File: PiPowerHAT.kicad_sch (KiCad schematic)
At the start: 31 parts, among them J3 Conn_01x02, J8 Conn_01x02

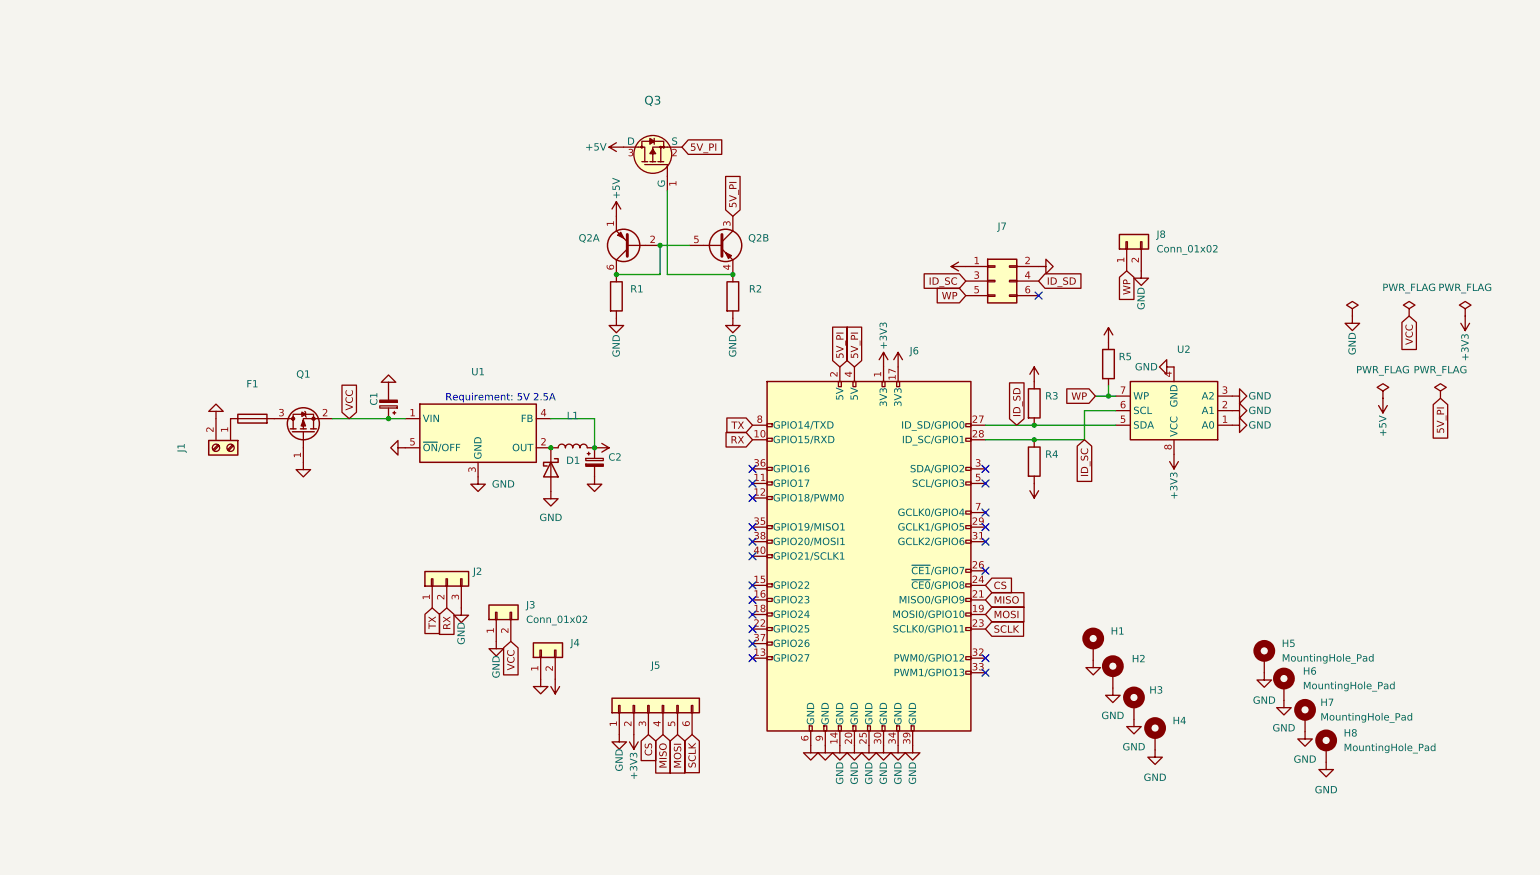
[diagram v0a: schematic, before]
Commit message: Updating to add freewheeling diodes, power LEDs, etc.
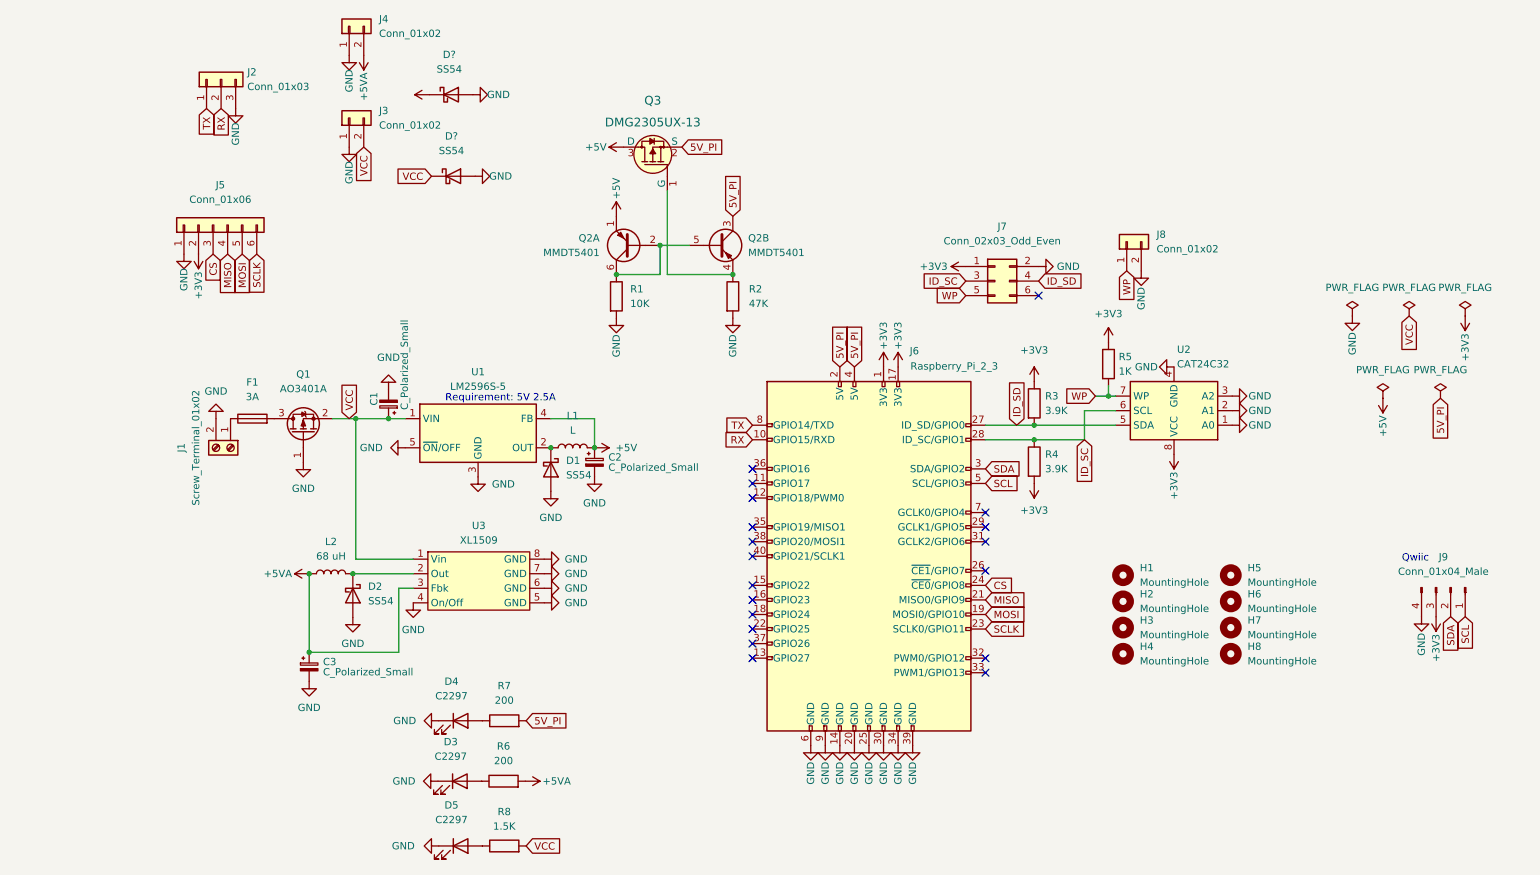
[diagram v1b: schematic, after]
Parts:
- removed H1, H2, H3, H4: (no value), symbol Mechanical:MountingHole_Pad
- removed H5, H6, H7, H8: MountingHole_Pad, symbol Mechanical:MountingHole_Pad
- added C3: C_Polarized_Small, symbol Device:C_Polarized_Small
- added D2, D? (x2): SS54, symbol Device:D_Schottky
- added D3, D4, D5: C2297, LED_SMD:LED_0805_2012Metric, symbol Device:LED
- added H1, H2, H3, H4, H5, H6, H7, H8: MountingHole, symbol Mechanical:MountingHole
- added J9: Conn_01x04_Male, symbol Connector:Conn_01x04_Male
- added L2: 68 uH, symbol Device:L
- added R6, R7: 200, symbol Device:R
- added R8: 1.5K, symbol Device:R
- added U3: XL1509, Package_SO:SOIC-8_3.9x4.9mm_P1.27mm, symbol Regulator_Switching:XL1509
- C1, C2: value (none) -> C_Polarized_Small
- D1: value (none) -> SS54
- F1: value (none) -> 3A
- J1: value (none) -> Screw_Terminal_01x02
- J2: value (none) -> Conn_01x03
- J4: value (none) -> Conn_01x02
- J5: value (none) -> Conn_01x06
- J6: value (none) -> Raspberry_Pi_2_3
- J7: value (none) -> Conn_02x03_Odd_Even
- L1: value (none) -> L
- Q1: value (none) -> AO3401A; footprint (none) -> Package_TO_SOT_SMD:SOT-23
- Q2: value (none) -> MMDT5401; footprint (none) -> Package_TO_SOT_SMD:SOT-363_SC-70-6
- Q3: value (none) -> DMG2305UX-13; footprint (none) -> digikey-footprints:SOT-23-3
- R1: value (none) -> 10K
- R2: value (none) -> 47K
- R3, R4: value (none) -> 3.9K
- R5: value (none) -> 1K
- U1: value (none) -> LM2596S-5; footprint (none) -> Package_TO_SOT_SMD:TO-263-5_TabPin3
- U2: value (none) -> CAT24C32
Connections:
- net +3V3: now also J9.3 (Pin_3)
- net +5V: no longer J4.2 (Pin_2)
- net 5V_PI: now also R7.2
- net GND: now also C3.2, D2.2 (A), D3.1 (K), D4.1 (K), D5.1 (K), D?.2 (A), D?.2 (A), J9.4 (Pin_4), U3.4 (On/Off), U3.5 (GND), U3.6 (GND), U3.7 (GND), U3.8 (GND)
- net VCC: now also D?.1 (K), R8.2, U3.1 (Vin)
- net SDA: now reaches J6.3 (SDA/GPIO2)
- net SDA: now also J9.2 (Pin_2)
- net SCL: now reaches J6.5 (SCL/GPIO3)
- net SCL: now also J9.1 (Pin_1)
- new net: D3.2 (A), R6.1
- new net: D2.1 (K), L2.2, U3.2 (Out)
- new net: D5.2 (A), R8.1
- new net: D4.2 (A), R7.1
- new net +5VA: C3.1, D?.1 (K), J4.2 (Pin_2), L2.1, R6.2, U3.3 (Fbk)
- no-connect marks 21 -> 19
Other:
- note added: "Qwiic"
- moved on the sheet: J2, J3, J4, J5

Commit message: adding footprints assignment to sch
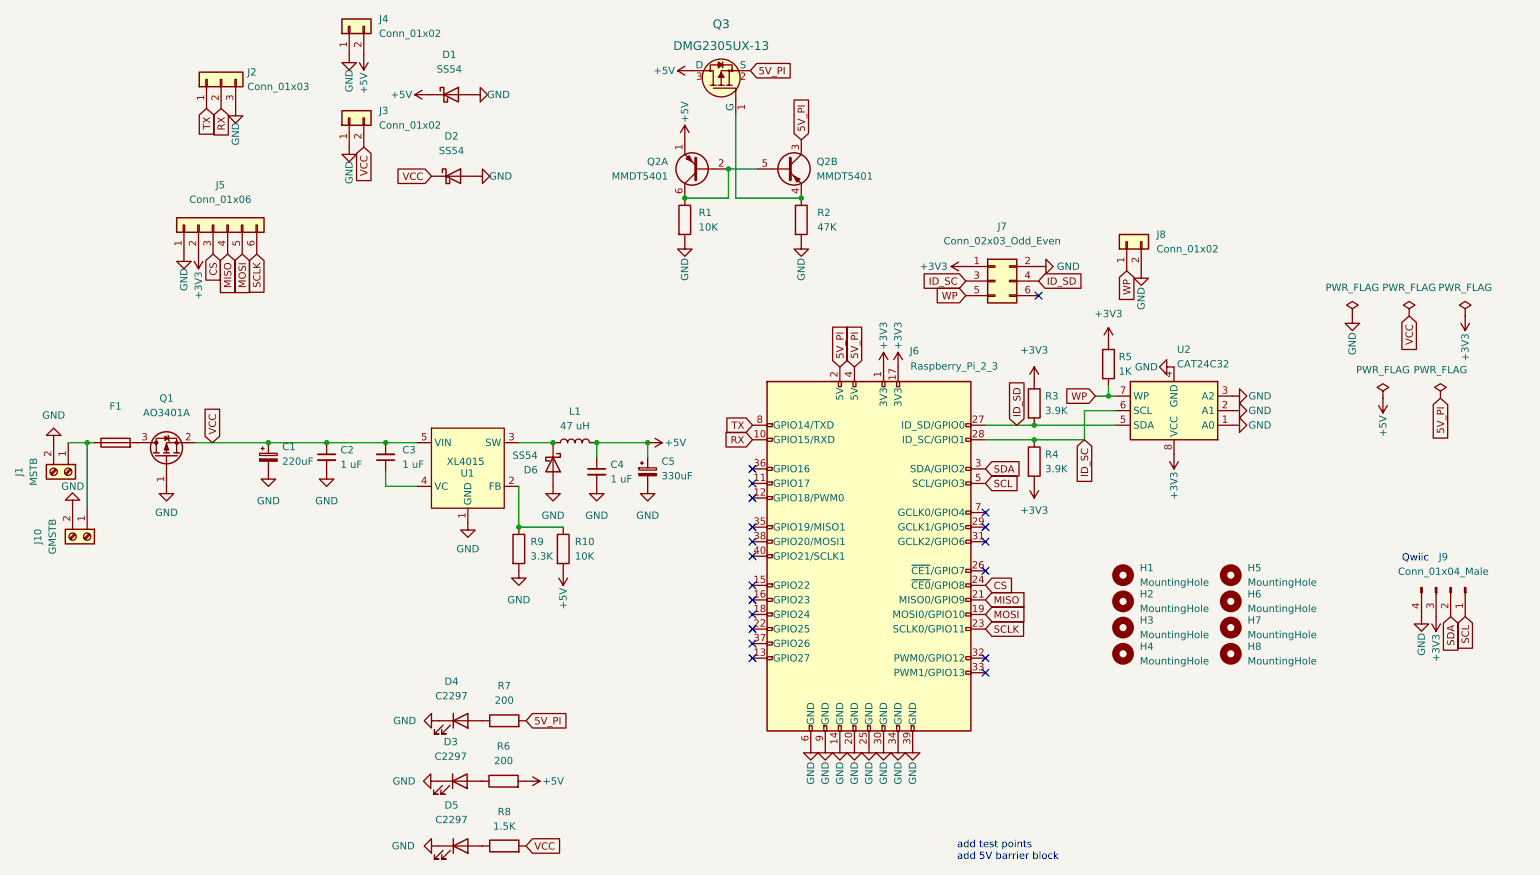
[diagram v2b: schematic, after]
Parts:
- removed C2, C3: C_Polarized_Small, symbol Device:C_Polarized_Small
- removed D1, D2: SS54, symbol Device:D_Schottky
- removed L2: 68 uH, symbol Device:L
- removed U1: LM2596S-5, Package_TO_SOT_SMD:TO-263-5_TabPin3, symbol Regulator_Switching:LM2596S-5
- removed U3: XL1509, Package_SO:SOIC-8_3.9x4.9mm_P1.27mm, symbol Regulator_Switching:XL1509
- added C2, C3, C4: 1 uF, Capacitor_SMD:C_0201_0603Metric, symbol Device:C_Small
- added C5: 330uF, Capacitor_SMD:CP_Elec_6.3x7.7, symbol Device:C_Polarized_Small
- added D6: SS54, Diode_SMD:D_SMA, symbol Device:D_Schottky
- added J10: GMSTB, Connector_Phoenix_GMSTB:PhoenixContact_GMSTBVA_2,5_2-G-7,62_1x02_P7.62mm_Vertical, symbol Connector:Screw_Terminal_01x02
- added R10: 10K, Resistor_SMD:R_0402_1005Metric, symbol Device:R
- added R9: 3.3K, Resistor_SMD:R_0402_1005Metric, symbol Device:R
- added U1: XL4015, Package_TO_SOT_SMD:TO-263-5_TabPin3, symbol Regulator_Switching:XL4015
- C1: value C_Polarized_Small -> 220uF; footprint (none) -> Capacitor_SMD:CP_Elec_10x10; JLC (none) -> C176670
- D1, D2: renamed from D?; footprint (none) -> Diode_SMD:D_SMA
- F1: value 3A -> (none); Farnell (none) -> 2292904
- H1, H2, H3, H4: footprint (none) -> MountingHole:MountingHole_2.7mm_M2.5_ISO14580
- H5, H6, H7, H8: footprint (none) -> MountingHole:MountingHole_3.5mm
- J1: value Screw_Terminal_01x02 -> MSTB; footprint (none) -> Connector_Phoenix_MSTB:PhoenixContact_MSTBVA_2,5_2-G_1x02_P5.00mm_Vertical
- J2: footprint (none) -> Connector_PinHeader_2.54mm:PinHeader_1x03_P2.54mm_Vertical
- J3, J4: footprint (none) -> Connector_JST:JST_XH_B2B-XH-AM_1x02_P2.50mm_Vertical
- J5: footprint (none) -> Connector_PinHeader_2.54mm:PinHeader_1x06_P2.54mm_Vertical
- J6: footprint (none) -> Connector_PinHeader_2.54mm:PinHeader_2x20_P2.54mm_Vertical
- J7: footprint (none) -> Connector_PinHeader_2.54mm:PinHeader_2x03_P2.54mm_Vertical_SMD
- J8: footprint (none) -> Connector_PinHeader_2.54mm:PinHeader_1x02_P2.54mm_Vertical
- J9: footprint (none) -> Connector_PinHeader_2.54mm:PinHeader_1x04_P2.54mm_Vertical
- L1: value L -> 47 uH; footprint (none) -> Inductor_SMD:L_12x12mm_H6mm; JLC (none) -> YSPI1365-470M
- R1: footprint (none) -> Resistor_SMD:R_0402_1005Metric
- R2: footprint (none) -> Resistor_SMD:R_0402_1005Metric; JLC (none) -> C25792
- R3, R4: footprint (none) -> Resistor_SMD:R_0402_1005Metric; JLC (none) -> C51721
- R5: footprint (none) -> Resistor_SMD:R_0402_1005Metric; JLC (none) -> C11702
- R6, R7: footprint (none) -> Resistor_SMD:R_0402_1005Metric; JLC (none) -> C25087
- R8: footprint (none) -> Resistor_SMD:R_0402_1005Metric; JLC (none) -> C25867
- U2: footprint (none) -> Package_SO:SOIC-8_3.9x4.9mm_P1.27mm
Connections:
- net +5VA is gone; now on net +5V: D1.1 (K), J4.2 (Pin_2), R6.2
- net +5V: now also C4.1, C5.1, R10.2
- net GND: now also C2.2, C4.2, C5.2, D6.2 (A), J10.2 (Pin_2), R9.2, U1.1 (GND)
- net VCC: now also C2.1, C3.2, U1.5 (VIN)
- net at F1.1, J1.1 (Pin_1): now also J10.1 (Pin_1)
- net at L1.1: now also D6.1 (K), U1.3 (SW)
- new net: C3.1, U1.4 (VC)
- new net: R10.1, R9.1, U1.2 (FB)
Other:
- note added: "add test points add 5V barrier block"
- note removed: "Requirement: 5V 2.5A"
- moved on the sheet: F1, J1, Q1, Q2A, Q2B, Q3, R1, R2

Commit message: currently under development. Layout in progress
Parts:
- removed D1: SS54, Diode_SMD:D_SMA, symbol Device:D_Schottky
- removed D4: C2297, LED_SMD:LED_0805_2012Metric, symbol Device:LED
- removed J4: Conn_01x02, Connector_JST:JST_XH_B2B-XH-AM_1x02_P2.50mm_Vertical, symbol Connector_Generic:Conn_01x02
- removed J8: Conn_01x02, Connector_PinHeader_2.54mm:PinHeader_1x02_P2.54mm_Vertical, symbol Connector_Generic:Conn_01x02
- removed R7: 200, Resistor_SMD:R_0402_1005Metric, symbol Device:R
- added JP1: SolderJumper_3_Bridged12, Jumper:SolderJumper-3_P1.3mm_Bridged2Bar12_RoundedPad1.0x1.5mm, symbol Jumper:SolderJumper_3_Bridged12
- C2, C3, C4: footprint Capacitor_SMD:C_0201_0603Metric -> Capacitor_SMD:C_0603_1608Metric
- F1: value (none) -> 5A; footprint (none) -> Fuse:Fuseholder_Blade_Keystone_3557-2
- R10: footprint Resistor_SMD:R_0402_1005Metric -> Resistor_SMD:R_0603_1608Metric; JLC C25744 -> C25804
- R9: footprint Resistor_SMD:R_0402_1005Metric -> Resistor_SMD:R_0603_1608Metric; JLC C25890 -> C22978
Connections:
- net +5V: now also JP1.3 (B)
- net VCC: now also JP1.1 (A); no longer D2.1 (K), J3.2 (Pin_2)
- new net: D2.1 (K), J3.2 (Pin_2), JP1.2 (C)
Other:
- note removed: "Qwiic"
- moved on the sheet: D2

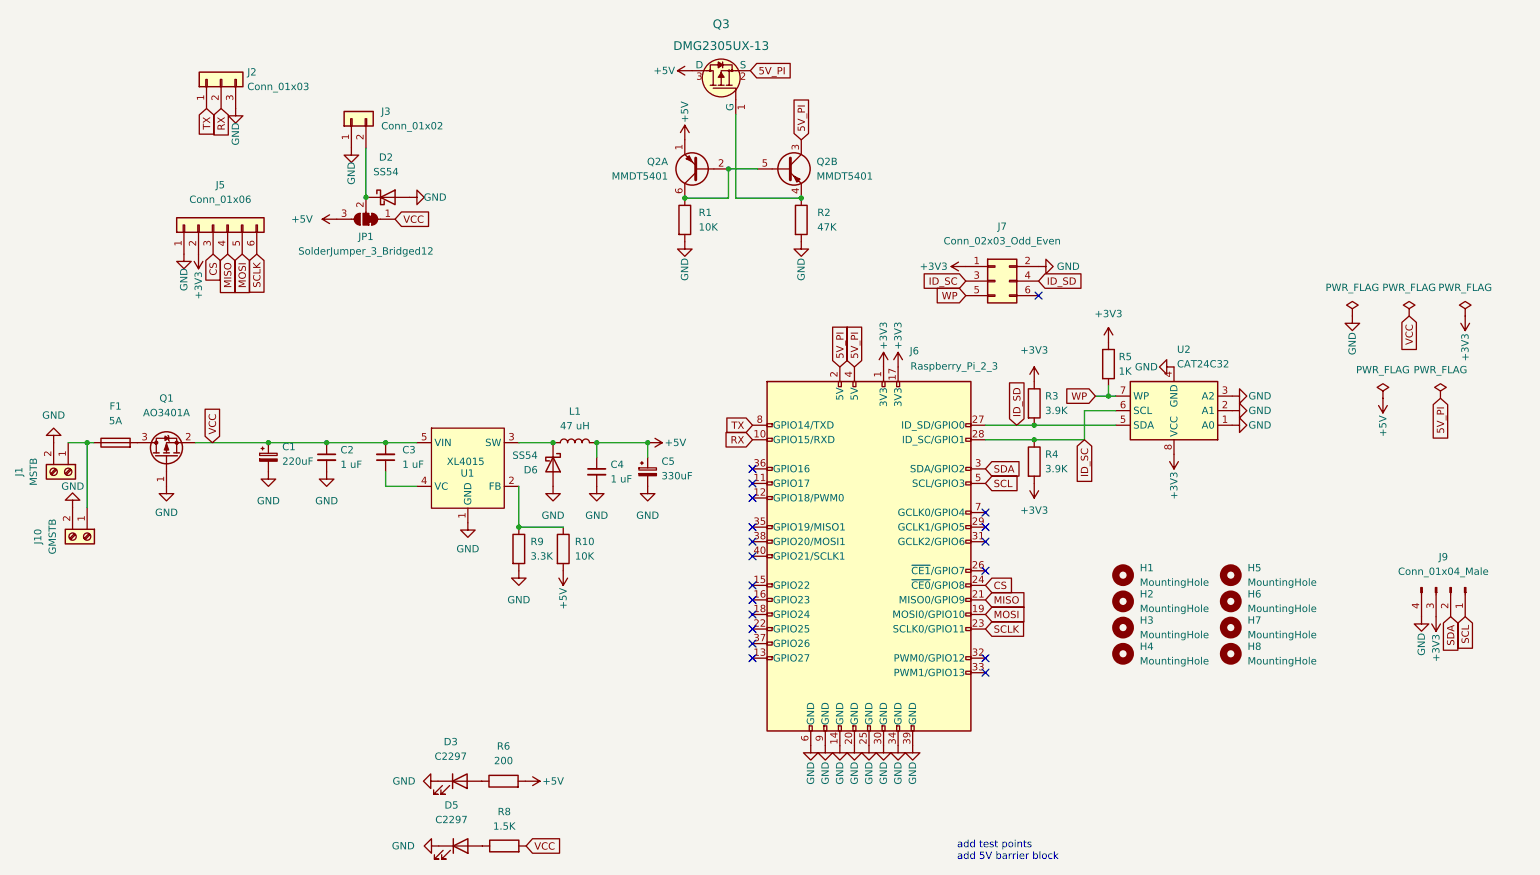
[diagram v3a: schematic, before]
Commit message: changed out fuseholder, mounting holes, headers, removed i2c, etc
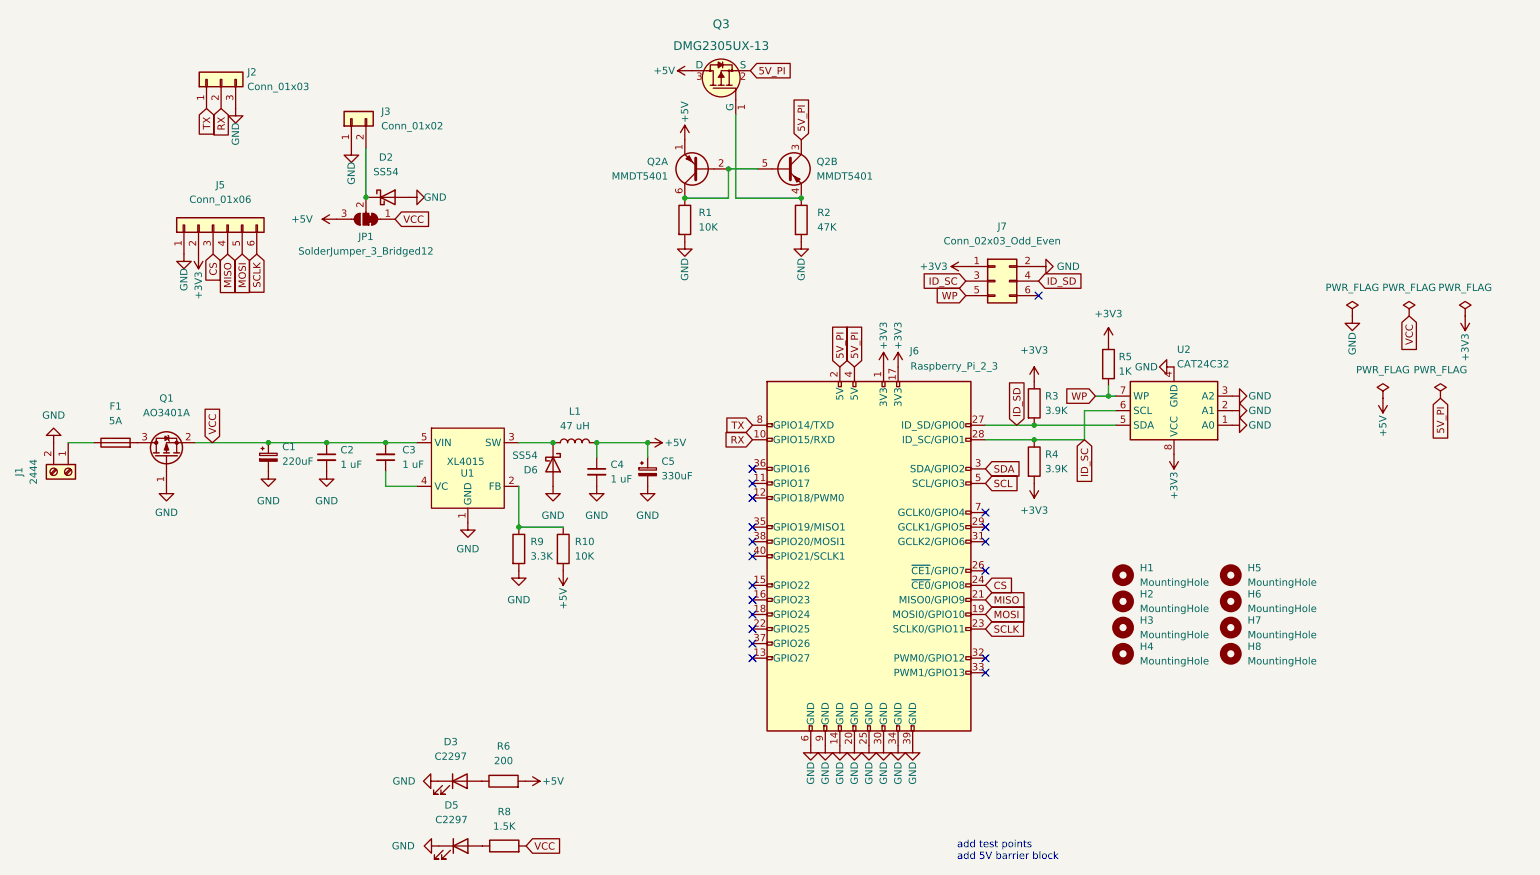
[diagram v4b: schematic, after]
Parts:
- removed J10: GMSTB, Connector_Phoenix_GMSTB:PhoenixContact_GMSTBVA_2,5_2-G-7,62_1x02_P7.62mm_Vertical, symbol Connector:Screw_Terminal_01x02
- removed J9: Conn_01x04_Male, Connector_PinHeader_2.54mm:PinHeader_1x04_P2.54mm_Vertical, symbol Connector:Conn_01x04_Male
- F1: footprint Fuse:Fuseholder_Blade_Keystone_3557-2 -> Fuse:Fuseholder_Littelfuse_Nano2_154x
- H1, H2, H3, H4: footprint MountingHole:MountingHole_2.7mm_M2.5_ISO14580 -> MountingHole:MountingHole_2.7mm_M2.5_DIN965_Pad
- J1: value MSTB -> 2444; footprint Connector_Phoenix_MSTB:PhoenixContact_MSTBVA_2,5_2-G_1x02_P5.00mm_Vertical -> TerminalBlock_4Ucon:TerminalBlock_4Ucon_1x02_P3.50mm_Horizontal
- J2: footprint Connector_PinHeader_2.54mm:PinHeader_1x03_P2.54mm_Vertical -> Connector_PinHeader_2.54mm:PinHeader_1x03_P2.54mm_Vertical_SMD_Pin1Left
- J5: footprint Connector_PinHeader_2.54mm:PinHeader_1x06_P2.54mm_Vertical -> Connector_PinHeader_2.54mm:PinHeader_1x06_P2.54mm_Vertical_SMD_Pin1Left
